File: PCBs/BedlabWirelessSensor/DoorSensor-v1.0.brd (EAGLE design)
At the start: 43.2 x 51.1 mm, 19 parts, among them U1 ATMEGA328P_PDIP

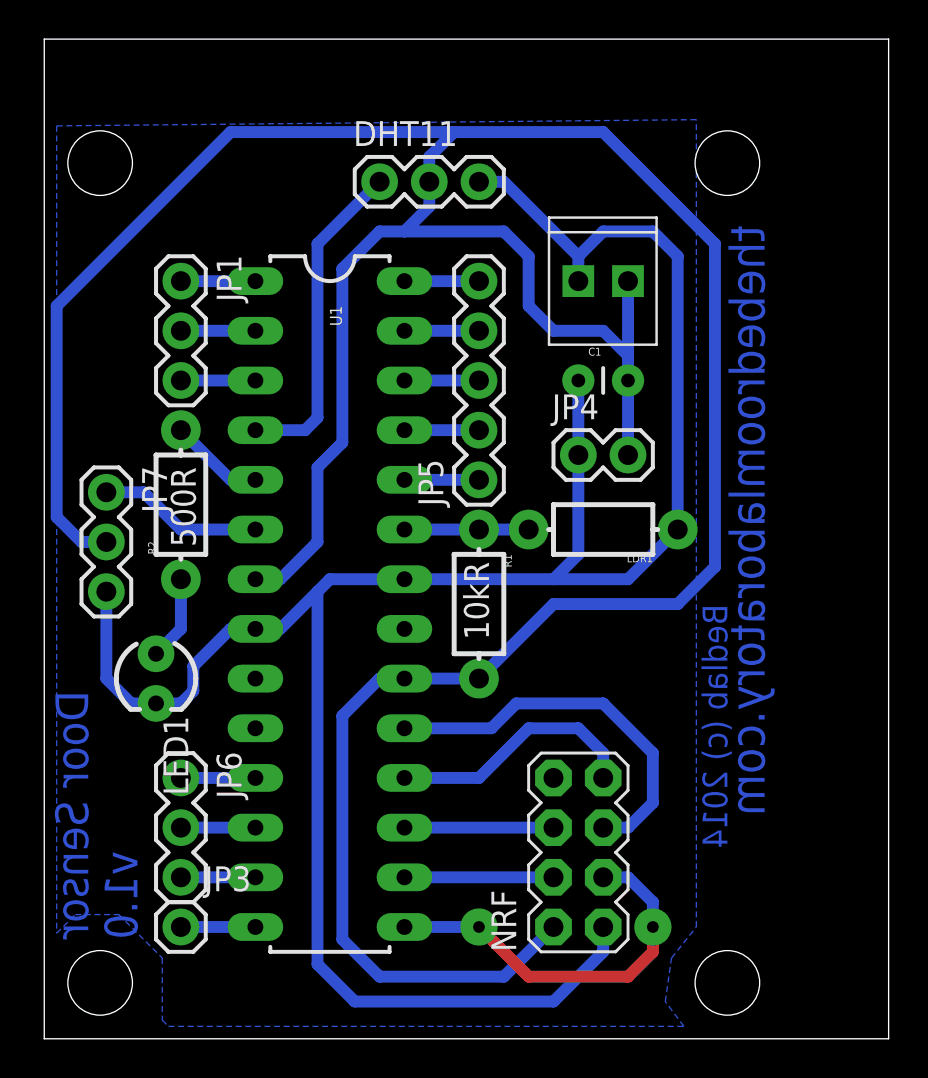
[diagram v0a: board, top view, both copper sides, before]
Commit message: Tiled PCB layout added for printing tomorrow. Additionally, changes made to arduino sketches to add funtionality for LDR, LED, Temp/humid sensor and switching the lights on/off from the gateway.
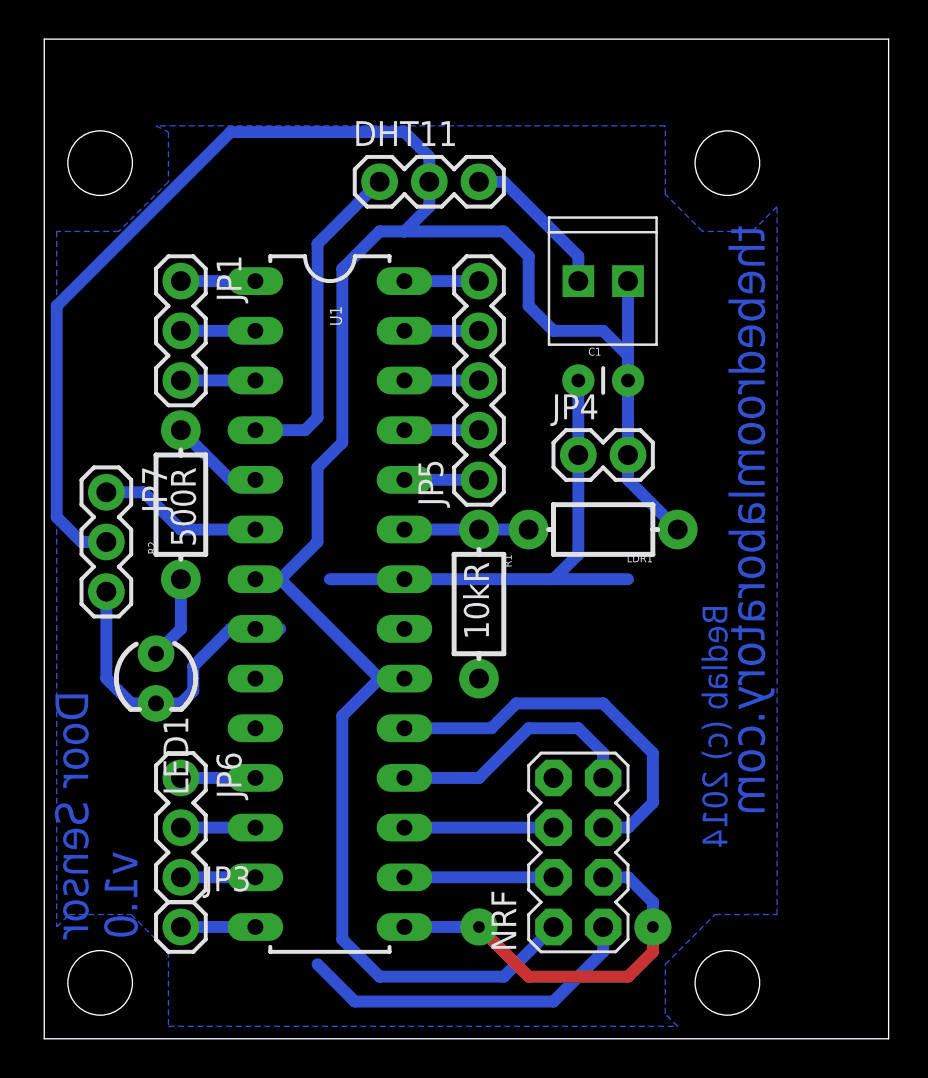
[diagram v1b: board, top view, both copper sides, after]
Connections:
- net GND: now also R1.P$2; no longer LDR1.P$1
- net VCC: now also LDR1.P$1; no longer R1.P$2
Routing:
- net GND: track 114.1 -> 67.8 mm
- net VCC: track 169.3 -> 128.4 mm
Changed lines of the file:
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@@
 <grid distance="0.0125" unitdist="inch" unit="inch" style="lines" multiple="1" display="yes" altdistance="0.025" altunitdist="inch" altunit="inch"/>
 <layers>
-<layer number="1" name="Top" color="4" fill="1" visible="yes" active="yes"/>
+<layer number="1" name="Top" color="4" fill="1" visible="no" active="yes"/>
 <layer number="16" name="Bottom" color="1" fill="1" visible="yes" active="yes"/>
 <layer number="17" name="Pads" color="2" fill="1" visible="yes" active="yes"/>
 <layer number="18" name="Vias" color="2" fill="1" visible="yes" active="yes"/>
-<layer number="19" name="Unrouted" color="6" fill="1" visible="yes" active="yes"/>
+<layer number="19" name="Unrouted" color="6" fill="1" visible="no" active="yes"/>
 <layer number="20" name="Dimension" color="15" fill="1" visible="yes" active="yes"/>
-<layer number="21" name="tPlace" color="7" fill="1" visible="yes" active="yes"/>
-<layer number="22" name="bPlace" color="7" fill="1" visible="yes" active="yes"/>
-<layer number="23" name="tOrigins" color="15" fill="1" visible="yes" active="yes"/>
-<layer number="24" name="bOrigins" color="15" fill="1" visible="yes" active="yes"/>
-<layer number="25" name="tNames" color="7" fill="1" visible="yes" active="yes"/>
-<layer number="26" name="bNames" color="7" fill="1" visible="yes" active="yes"/>
-<layer number="27" name="tValues" color="7" fill="1" visible="yes" active="yes"/>
-<layer number="28" name="bValues" color="7" fill="1" visible="yes" active="yes"/>
+<layer number="21" name="tPlace" color="7" fill="1" visible="no" active="yes"/>
+<layer number="22" name="bPlace" color="7" fill="1" visible="no" active="yes"/>
+<layer number="23" name="tOrigins" color="15" fill="1" visible="no" active="yes"/>
+<layer number="24" name="bOrigins" color="15" fill="1" visible="no" active="yes"/>
+<layer number="25" name="tNames" color="7" fill="1" visible="no" active="yes"/>
+<layer number="26" name="bNames" color="7" fill="1" visible="no" active="yes"/>
+<layer number="27" name="tValues" color="7" fill="1" visible="no" active="yes"/>
+<layer number="28" name="bValues" color="7" fill="1" visible="no" active="yes"/>
 <layer number="29" name="tStop" color="7" fill="3" visible="no" active="yes"/>
 <layer number="30" name="bStop" color="7" fill="6" visible="no" active="yes"/>
@@
 <layer number="37" name="tTest" color="7" fill="1" visible="no" active="yes"/>
 <layer number="38" name="bTest" color="7" fill="1" visible="no" active="yes"/>
-<layer number="39" name="tKeepout" color="4" fill="11" visible="yes" active="yes"/>
-<layer number="40" name="bKeepout" color="1" fill="11" visible="yes" active="yes"/>
-<layer number="41" name="tRestrict" color="4" fill="10" visible="yes" active="yes"/>
-<layer number="42" name="bRestrict" color="1" fill="10" visible="yes" active="yes"/>
-<layer number="43" name="vRestrict" color="2" fill="10" visible="yes" active="yes"/>
+<layer number="39" name="tKeepout" color="4" fill="11" visible="no" active="yes"/>
+<layer number="40" name="bKeepout" color="1" fill="11" visible="no" active="yes"/>
+<layer number="41" name="tRestrict" color="4" fill="10" visible="no" active="yes"/>
+<layer number="42" name="bRestrict" color="1" fill="10" visible="no" active="yes"/>
+<layer number="43" name="vRestrict" color="2" fill="10" visible="no" active="yes"/>
 <layer number="44" name="Drills" color="7" fill="1" visible="no" active="yes"/>
 <layer number="45" name="Holes" color="7" fill="1" visible="no" active="yes"/>
 <layer number="46" name="Milling" color="3" fill="1" visible="no" active="yes"/>
 <layer number="47" name="Measures" color="7" fill="1" visible="no" active="yes"/>
-<layer number="48" name="Document" color="7" fill="1" visible="yes" active="yes"/>
-<layer number="49" name="Reference" color="7" fill="1" visible="yes" active="yes"/>
+<layer number="48" name="Document" color="7" fill="1" visible="no" active="yes"/>
+<layer number="49" name="Reference" color="7" fill="1" visible="no" active="yes"/>
 <layer number="50" name="dxf" color="7" fill="1" visible="no" active="no"/>
-<layer number="51" name="tDocu" color="7" fill="1" visible="yes" active="yes"/>
-<layer number="52" name="bDocu" color="7" fill="1" visible="yes" active="yes"/>
+<layer number="51" name="tDocu" color="7" fill="1" visible="no" active="yes"/>
+<layer number="52" name="bDocu" color="7" fill="1" visible="no" active="yes"/>
 <layer number="53" name="tGND_GNDA" color="7" fill="9" visible="no" active="no"/>
 <layer number="54" name="bGND_GNDA" color="1" fill="9" visible="no" active="no"/>
@@
 </signal>
 <signal name="VCC">
-<contactref element="R1" pad="P$2"/>
 <contactref element="DHT11" pad="2"/>
 <contactref element="U1" pad="20"/>
@@
 <wire x1="15.24" y1="5.08" x2="15.24" y2="16.51" width="0.6096" layer="16"/>
 <wire x1="15.24" y1="16.51" x2="17.145" y2="18.415" width="0.6096" layer="16"/>
-<wire x1="17.145" y1="18.415" x2="18.415" y2="18.415" width="0.6096" layer="16"/>
 <wire x1="29.845" y1="33.655" x2="29.845" y2="34.925" width="0.6096" layer="16"/>
 <wire x1="29.845" y1="38.735" x2="29.845" y2="34.925" width="0.6096" layer="16"/>
@@
 <wire x1="13.97" y1="29.21" x2="15.24" y2="30.48" width="0.6096" layer="16"/>
 <wire x1="15.24" y1="30.48" x2="15.24" y2="39.37" width="0.6096" layer="16"/>
-<wire x1="22.225" y1="18.415" x2="26.035" y2="22.225" width="0.6096" layer="16"/>
-<wire x1="26.035" y1="22.225" x2="32.385" y2="22.225" width="0.6096" layer="16"/>
-<wire x1="32.385" y1="22.225" x2="34.29" y2="24.13" width="0.6096" layer="16"/>
-<wire x1="34.29" y1="24.13" x2="34.29" y2="40.64" width="0.6096" layer="16"/>
-<wire x1="34.29" y1="40.64" x2="28.575" y2="46.355" width="0.6096" layer="16"/>
-<wire x1="28.575" y1="46.355" x2="20.955" y2="46.355" width="0.6096" layer="16"/>
-<wire x1="20.955" y1="46.355" x2="19.685" y2="45.085" width="0.6096" layer="16"/>
 <wire x1="19.685" y1="45.085" x2="19.685" y2="43.815" width="0.6096" layer="16"/>
-<wire x1="18.415" y1="18.415" x2="22.225" y2="18.415" width="0.6096" layer="16"/>
 <contactref element="JP7" pad="2"/>
 <wire x1="3.175" y1="25.4" x2="1.905" y2="25.4" width="0.6096" layer="16"/>
@@
 <wire x1="0.635" y1="26.67" x2="0.635" y2="37.465" width="0.6096" layer="16"/>
 <wire x1="0.635" y1="37.465" x2="9.525" y2="46.355" width="0.6096" layer="16"/>
-<wire x1="9.525" y1="46.355" x2="20.955" y2="46.355" width="0.6096" layer="16"/>
+<contactref element="LDR1" pad="P$1"/>
+<wire x1="19.685" y1="45.085" x2="18.415" y2="46.355" width="0.6096" layer="16"/>
+<wire x1="18.415" y1="46.355" x2="9.525" y2="46.355" width="0.6096" layer="16"/>
+<wire x1="32.385" y1="26.035" x2="29.845" y2="28.575" width="0.6096" layer="16"/>
+<wire x1="29.845" y1="28.575" x2="29.845" y2="29.845" width="0.6096" layer="16"/>
+<wire x1="12.065" y1="23.495" x2="17.145" y2="18.415" width="0.6096" layer="16"/>
+<wire x1="17.145" y1="18.415" x2="18.415" y2="18.415" width="0.6096" layer="16"/>
 </signal>
 <signal name="GND">
-<contactref element="LDR1" pad="P$1"/>
 <contactref element="DHT11" pad="3"/>
 <contactref element="U1" pad="8"/>
@@
 <wire x1="27.305" y1="24.765" x2="26.035" y2="23.495" width="0.6096" layer="16"/>
 <wire x1="26.035" y1="23.495" x2="18.415" y2="23.495" width="0.6096" layer="16"/>
-<wire x1="32.385" y1="26.035" x2="29.845" y2="23.495" width="0.6096" layer="16"/>
 <wire x1="29.845" y1="23.495" x2="26.035" y2="23.495" width="0.6096" layer="16"/>
 <wire x1="27.305" y1="38.735" x2="27.305" y2="40.005" width="0.6096" layer="16"/>
-<wire x1="27.305" y1="40.005" x2="28.575" y2="41.275" width="0.6096" layer="16"/>
-<wire x1="28.575" y1="41.275" x2="31.115" y2="41.275" width="0.6096" layer="16"/>
-<wire x1="31.115" y1="41.275" x2="32.385" y2="40.005" width="0.6096" layer="16"/>
-<wire x1="32.385" y1="40.005" x2="32.385" y2="26.035" width="0.6096" layer="16"/>
 <wire x1="27.305" y1="40.005" x2="23.495" y2="43.815" width="0.6096" layer="16"/>
 <wire x1="23.495" y1="43.815" x2="22.225" y2="43.815" width="0.6096" layer="16"/>
 <wire x1="15.875" y1="1.905" x2="13.97" y2="3.81" width="0.6096" layer="16"/>
-<wire x1="13.97" y1="3.81" x2="13.97" y2="22.86" width="0.6096" layer="16"/>
-<wire x1="13.97" y1="22.86" x2="12.065" y2="20.955" width="0.6096" layer="16"/>
 <wire x1="12.065" y1="20.955" x2="10.795" y2="20.955" width="0.6096" layer="16"/>
-<wire x1="18.415" y1="23.495" x2="14.605" y2="23.495" width="0.6096" layer="16"/>
-<wire x1="14.605" y1="23.495" x2="13.97" y2="22.86" width="0.6096" layer="16"/>
 <wire x1="28.575" y1="5.715" x2="28.575" y2="4.445" width="0.6096" layer="16"/>
 <wire x1="28.575" y1="4.445" x2="26.035" y2="1.905" width="0.6096" layer="16"/>
@@
 <wire x1="7.62" y1="19.05" x2="9.525" y2="20.955" width="0.6096" layer="16"/>
 <wire x1="9.525" y1="20.955" x2="10.795" y2="20.955" width="0.6096" layer="16"/>
+<contactref element="R1" pad="P$2"/>
+<wire x1="14.605" y1="23.495" x2="18.415" y2="23.495" width="0.6096" layer="16"/>
 <polygon width="0.3048" layer="16">
-<vertex x="0.635" y="46.6725"/>
-<vertex x="0.635" y="5.3975"/>
-<vertex x="1.5875" y="6.35"/>
-<vertex x="3.81" y="6.35"/>
-<vertex x="6.0325" y="4.1275"/>
-<vertex x="6.0325" y="0.9525"/>
+<vertex x="5.715" y="46.6725"/>
+<vertex x="6.35" y="46.355"/>
+<vertex x="6.35" y="43.815"/>
+<vertex x="3.81" y="41.275"/>
+<vertex x="0.635" y="41.275"/>
+<vertex x="0.635" y="5.715"/>
+<vertex x="1.27" y="6.35"/>
+<vertex x="4.445" y="6.35"/>
+<vertex x="6.35" y="4.445"/>
 <vertex x="6.35" y="0.635"/>
-<vertex x="32.7025" y="0.635"/>
-<vertex x="31.75" y="1.905"/>
-<vertex x="32.0675" y="4.1275"/>
-<vertex x="33.3375" y="5.715"/>
-<vertex x="33.3375" y="46.99"/>
+<vertex x="32.385" y="0.635"/>
+<vertex x="31.75" y="1.27"/>
+<vertex x="31.75" y="3.81"/>
+<vertex x="34.29" y="6.35"/>
+<vertex x="37.465" y="6.35"/>
+<vertex x="37.465" y="42.545"/>
+<vertex x="36.195" y="41.275"/>
+<vertex x="33.655" y="41.275"/>
+<vertex x="31.75" y="43.18"/>
+<vertex x="31.75" y="46.6725"/>
 </polygon>
 </signal>
